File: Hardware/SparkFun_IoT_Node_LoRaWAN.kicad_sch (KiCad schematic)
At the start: 67 parts, among them J1 USB_C_Receptacle, J2 Conn_01x03, J3 USB_C_Receptacle, J4 SWD, SW1 DPDT_Slide_SMD_7.2x3.5mm, U1 RP2350A, U2 W25Q128JVPIM, U3 APS6404L-3SQR-ZR, U4 XBLR, U5 CH340C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

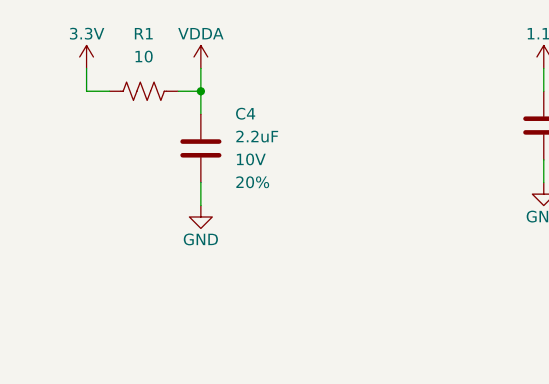
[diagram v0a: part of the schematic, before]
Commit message: Cosmetic tweaks
Nudge IO 29 silk away from mounting hole
Add VDDA RC filter cutoff frequency
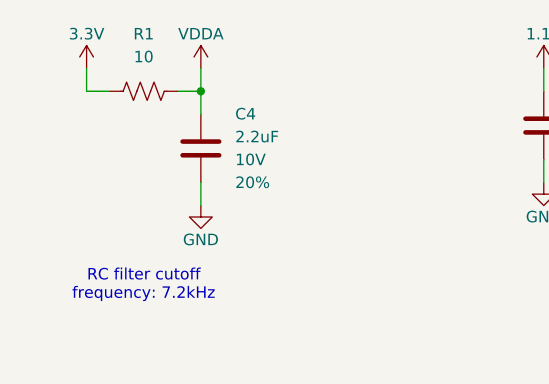
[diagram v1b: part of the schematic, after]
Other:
- note added: "RC filter cutoff frequency: 7.2kHz"
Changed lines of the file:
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@@
+		)
+	)
+	(text "RC filter cutoff\nfrequency: 7.2kHz"
+		(exclude_from_sim no)
+		(at 26.67 257.81 0)
+		(effects
+			(font
+				(size 1.27 1.27)
+			)
 		)
 	)

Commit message: Symbol and footprint update
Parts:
- J4: symbol SparkFun-Connector:Debug-Cortex-2x5-SMD-Unshrouded -> SparkFun-Connector:Debug-Cortex-2x5_P1.27mm-SMD-Unshrouded
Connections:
- net at J3.A8 (NC): no longer J3.B8 (NC)
- net at J1.A8 (NC): no longer J1.B8 (NC)
- now unconnected: J1.NC1 (NC), J1.NC2 (NC), J1.NC3 (NC), J3.NC1 (NC), J3.NC2 (NC), J3.NC3 (NC)
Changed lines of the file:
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@@
 	)
 	(symbol
-		(lib_name "USB_C_Receptacle_1")
 		(lib_id "SparkFun-Connector:USB_C_Receptacle")
 		(at 254 49.53 0)
@@
 	)
 	(symbol
-		(lib_name "VUSB_6")
 		(lib_id "SparkFun-PowerSymbol:VUSB")
 		(at 246.38 134.62 0)
@@
 	)
 	(symbol
-		(lib_name "GND_37")
 		(lib_id "SparkFun-PowerSymbol:GND")
 		(at 300.99 76.2 0)
@@
 	)
 	(symbol
-		(lib_name "GND_35")
 		(lib_id "SparkFun-PowerSymbol:GND")
 		(at 71.12 220.98 0)
@@
 	)
 	(symbol
-		(lib_name "GND_33")
 		(lib_id "SparkFun-PowerSymbol:GND")
 		(at 259.08 147.32 0)
@@
 	)
 	(symbol
-		(lib_name "GND_34")
 		(lib_id "SparkFun-PowerSymbol:GND")
 		(at 30.48 175.26 0)
@@
 	)
 	(symbol
-		(lib_name "3.3V_23")
 		(lib_id "SparkFun-PowerSymbol:3.3V")
 		(at 193.04 121.92 0)
@@
 	)
 	(symbol
-		(lib_name "GND_36")
 		(lib_id "SparkFun-PowerSymbol:GND")
 		(at 279.4 142.24 0)
@@
 	)
 	(symbol
-		(lib_name "GND_29")
 		(lib_id "SparkFun-PowerSymbol:GND")
 		(at 144.78 233.68 0)
@@
 	)
 	(symbol
-		(lib_name "3.3V_18")
 		(lib_id "SparkFun-PowerSymbol:3.3V")
 		(at 58.42 208.28 0)
@@
 	)
 	(symbol
-		(lib_name "3.3V_19")
 		(lib_id "SparkFun-PowerSymbol:3.3V")
 		(at 185.42 208.28 0)
@@
 	)
 	(symbol
-		(lib_name "Standoff_2")
 		(lib_id "SparkFun-Hardware:Standoff")
 		(at 400.05 242.57 0)
@@
 	)
 	(symbol
-		(lib_name "GND_23")
 		(lib_id "SparkFun-PowerSymbol:GND")
 		(at 40.64 73.66 0)
@@
 	)
 	(symbol
-		(lib_name "3.3V_20")
 		(lib_id "SparkFun-PowerSymbol:3.3V")
 		(at 83.82 208.28 0)
@@
 	)
 	(symbol
-		(lib_name "3.3V_22")
 		(lib_id "SparkFun-PowerSymbol:3.3V")
 		(at 152.4 134.62 0)
@@
 	)
 	(symbol
-		(lib_name "Standoff_3")
 		(lib_id "SparkFun-Hardware:Standoff")
 		(at 403.86 242.57 0)
@@
 	)
 	(symbol
-		(lib_name "GND_28")
 		(lib_id "SparkFun-PowerSymbol:GND")
 		(at 33.02 248.92 0)
@@
 	)
 	(symbol
-		(lib_name "GND_27")
 		(lib_id "SparkFun-PowerSymbol:GND")
 		(at 241.3 228.6 0)
@@
 	)
 	(symbol
-		(lib_id "SparkFun-Connector:Debug-Cortex-2x5-SMD-Unshrouded")
+		(lib_id "SparkFun-Connector:Debug-Cortex-2x5_P1.27mm-SMD-Unshrouded")
 		(at 378.46 53.34 0)
 		(unit 1)
@@
 	)
 	(symbol
-		(lib_name "VUSB_4")
 		(lib_id "SparkFun-PowerSymbol:VUSB")
 		(at 300.99 48.26 0)
@@
 	)
 	(symbol
-		(lib_name "GND_30")
 		(lib_id "SparkFun-PowerSymbol:GND")
 		(at 45.72 220.98 0)
@@
 	)
 	(symbol
-		(lib_name "VUSB_5")
 		(lib_id "SparkFun-PowerSymbol:VUSB")
 		(at 284.48 38.1 0)
@@
 	)
 	(symbol
-		(lib_name "Standoff_1")
 		(lib_id "SparkFun-Hardware:Standoff")
 		(at 403.86 238.76 0)
@@
 	)
 	(symbol
-		(lib_name "3.3V_21")
 		(lib_id "SparkFun-PowerSymbol:3.3V")
 		(at 259.08 134.62 0)
@@
 	)
 	(symbol
-		(lib_name "GND_26")
 		(lib_id "SparkFun-PowerSymbol:GND")
 		(at 309.88 139.7 0)
@@
 	)
 	(symbol
-		(lib_name "GND_24")
 		(lib_id "SparkFun-PowerSymbol:GND")
 		(at 254 73.66 0)
@@
 	)
 	(symbol
-		(lib_name "GND_32")
 		(lib_id "SparkFun-PowerSymbol:GND")
 		(at 82.55 76.2 0)
@@
 	)
 	(symbol
-		(lib_name "GND_25")
 		(lib_id "SparkFun-PowerSymbol:GND")
 		(at 33.02 220.98 0)
@@
 	)
 	(symbol
-		(lib_name "GND_31")
 		(lib_id "SparkFun-PowerSymbol:GND")
 		(at 266.7 259.08 0)
@@
 	)
 	(symbol
-		(lib_name "GND_19")
 		(lib_id "SparkFun-PowerSymbol:GND")
 		(at 109.22 220.98 0)
@@
 	)
 	(symbol
-		(lib_name "GND_12")
 		(lib_id "SparkFun-PowerSymbol:GND")
 		(at 152.4 147.32 0)
@@
 	)
 	(symbol
-		(lib_name "Fiducial_0.5mm_1")
 		(lib_id "SparkFun-Aesthetic:Fiducial_0.5mm")
 		(at 411.48 242.57 0)
@@
 	)
 	(symbol
-		(lib_name "SolderJumper_2_Bridged_1")
 		(lib_id "SparkFun-Jumper:SolderJumper_2_Bridged")
 		(at 36.83 71.12 0)
@@
 	)
 	(symbol
-		(lib_name "GND_20")
 		(lib_id "SparkFun-PowerSymbol:GND")
 		(at 58.42 73.66 0)
@@
 	)
 	(symbol
-		(lib_name "3.3V_7")
 		(lib_id "SparkFun-PowerSymbol:3.3V")
 		(at 45.72 208.28 0)
@@
 	)
 	(symbol
-		(lib_name "3.3V_15")
 		(lib_id "SparkFun-PowerSymbol:3.3V")
 		(at 365.76 45.72 0)
@@
 	)
 	(symbol
-		(lib_name "VUSB_3")
 		(lib_id "SparkFun-PowerSymbol:VUSB")
 		(at 271.78 38.1 0)
@@
 	)
 	(symbol
-		(lib_name "GND_21")
 		(lib_id "SparkFun-PowerSymbol:GND")
 		(at 279.4 259.08 0)
@@
 	)
 	(symbol
-		(lib_name "3.3V_14")
 		(lib_id "SparkFun-PowerSymbol:3.3V")
 		(at 109.22 208.28 0)
@@
 	)
 	(symbol
-		(lib_name "GND_13")
 		(lib_id "SparkFun-PowerSymbol:GND")
 		(at 71.12 246.38 0)
@@
 	)
 	(symbol
-		(lib_name "3.3V_17")
 		(lib_id "SparkFun-PowerSymbol:3.3V")
 		(at 241.3 170.18 0)
@@
 	)
 	(symbol
-		(lib_name "3.3V_9")
 		(lib_id "SparkFun-PowerSymbol:3.3V")
 		(at 241.3 243.84 0)
@@
 	)
 	(symbol
-		(lib_name "GND_18")
 		(lib_id "SparkFun-PowerSymbol:GND")
 		(at 83.82 246.38 0)
@@
 	)
 	(symbol
-		(lib_name "GND_16")
 		(lib_id "SparkFun-PowerSymbol:GND")
 		(at 96.52 246.38 0)
@@
 	)
 	(symbol
-		(lib_name "GND_11")
 		(lib_id "SparkFun-PowerSymbol:GND")
 		(at 160.02 149.86 0)
@@
 	)
 	(symbol
-		(lib_name "3.3V_8")
 		(lib_id "SparkFun-PowerSymbol:3.3V")
 		(at 160.02 218.44 0)
@@
 	)
 	(symbol
-		(lib_name "Fiducial_0.5mm_2")
 		(lib_id "SparkFun-Aesthetic:Fiducial_0.5mm")
 		(at 411.48 238.76 0)
@@
 	)
 	(symbol
-		(lib_name "GND_14")
 		(lib_id "SparkFun-PowerSymbol:GND")
 		(at 58.42 220.98 0)
@@
 	)
 	(symbol
-		(lib_name "3.3V_11")
 		(lib_id "SparkFun-PowerSymbol:3.3V")
 		(at 96.52 208.28 0)
@@
 	)
 	(symbol
-		(lib_name "VDDA_1")
 		(lib_id "SparkFun-PowerSymbol:VDDA")
 		(at 33.02 233.68 0)
@@
 	)
 	(symbol
-		(lib_name "3.3V_13")
 		(lib_id "SparkFun-PowerSymbol:3.3V")
 		(at 63.5 109.22 0)
@@
 	)
 	(symbol
-		(lib_name "GND_10")
 		(lib_id "SparkFun-PowerSymbol:GND")
 		(at 246.38 147.32 0)
@@
 	)
 	(symbol
-		(lib_name "GND_22")
 		(lib_id "SparkFun-PowerSymbol:GND")
 		(at 152.4 233.68 0)
@@
 	)
 	(symbol
-		(lib_name "3.3V_16")
 		(lib_id "SparkFun-PowerSymbol:3.3V")
 		(at 276.86 106.68 0)
@@
 	)
 	(symbol
-		(lib_name "GND_9")
 		(lib_id "SparkFun-PowerSymbol:GND")
 		(at 109.22 246.38 0)
@@
 	)
 	(symbol
-		(lib_name "3.3V_10")
 		(lib_id "SparkFun-PowerSymbol:3.3V")
 		(at 33.02 208.28 0)
@@
 	)
 	(symbol
-		(lib_name "GND_8")
 		(lib_id "SparkFun-PowerSymbol:GND")
 		(at 83.82 220.98 0)
@@
 	)
 	(symbol
-		(lib_name "3.3V_6")
 		(lib_id "SparkFun-PowerSymbol:3.3V")
 		(at 279.4 243.84 0)
@@
 	)
 	(symbol
-		(lib_name "3.3V_12")
 		(lib_id "SparkFun-PowerSymbol:3.3V")
 		(at 160.02 132.08 0)
@@
 	)
 	(symbol
-		(lib_name "GND_7")
 		(lib_id "SparkFun-PowerSymbol:GND")
 		(at 271.78 73.66 0)
@@
 	)
 	(symbol
-		(lib_name "GND_17")
 		(lib_id "SparkFun-PowerSymbol:GND")
 		(at 20.32 220.98 0)
@@
 	)
 	(symbol
-		(lib_name "GND_15")
 		(lib_id "SparkFun-PowerSymbol:GND")
 		(at 365.76 58.42 0)
@@
 	)
 	(symbol
-		(lib_name "Fiducial_0.5mm_3")
 		(lib_id "SparkFun-Aesthetic:Fiducial_0.5mm")
 		(at 415.29 238.76 0)
@@
 	)
 	(symbol
-		(lib_name "VUSB_2")
 		(lib_id "SparkFun-PowerSymbol:VUSB")
 		(at 279.4 104.14 0)
@@
 	)
 	(symbol
-		(lib_name "3.3V_5")
 		(lib_id "SparkFun-PowerSymbol:3.3V")
 		(at 20.32 233.68 0)
@@
 	)
 	(symbol
-		(lib_name "3.3V_4")
 		(lib_id "SparkFun-PowerSymbol:3.3V")
 		(at 233.68 180.34 0)
@@
 	)
 	(symbol
-		(lib_name "GND_6")
 		(lib_id "SparkFun-PowerSymbol:GND")
 		(at 281.94 73.66 0)
@@
 	)
 	(symbol
-		(lib_name "GND_5")
 		(lib_id "SparkFun-PowerSymbol:GND")
 		(at 63.5 187.96 0)
@@
 	)
 	(symbol
-		(lib_name "3.3V_1")
 		(lib_id "SparkFun-PowerSymbol:3.3V")
 		(at 152.4 220.98 0)
@@
 	)
 	(symbol
-		(lib_name "GND_1")
 		(lib_id "SparkFun-PowerSymbol:GND")
 		(at 63.5 73.66 0)
@@
 	)
 	(symbol
-		(lib_name "3.3V_3")
 		(lib_id "SparkFun-PowerSymbol:3.3V")
 		(at 71.12 208.28 0)
@@
 	)
 	(symbol
-		(lib_name "GND_3")
 		(lib_id "SparkFun-PowerSymbol:GND")
 		(at 254 259.08 0)
@@
 	)
 	(symbol
-		(lib_name "GND_4")
 		(lib_id "SparkFun-PowerSymbol:GND")
 		(at 96.52 220.98 0)
@@
 	)
 	(symbol
-		(lib_name "GND_2")
 		(lib_id "SparkFun-PowerSymbol:GND")
 		(at 170.18 55.88 0)
@@
 	)
 	(symbol
-		(lib_name "VUSB_1")
 		(lib_id "SparkFun-PowerSymbol:VUSB")
 		(at 82.55 48.26 0)
@@
 	)
 	(symbol
-		(lib_name "3.3V_2")
 		(lib_id "SparkFun-PowerSymbol:3.3V")
 		(at 144.78 220.98 0)

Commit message: Design review updates
Fix layers to standard SFE usage
Add link to enclosure and PDF of dimensions
Move fiducials away from PTH pads
Add USB test points
Add XBLR debug test points
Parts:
- added TP10, TP3, TP4, TP5, TP6, TP7, TP8, TP9: 1.0mm, SparkFun-Connector:TestPoint-1.0mm, symbol SparkFun-Connector:TestPoint_1.0mm
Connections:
- net USB_D+: now also TP4.1
- net USB_D-: now also TP3.1
- net XBLR_SWCLK: now also TP6.1
- net XBLR_SWDIO: now also TP7.1
- net XBLR_SWO: now also TP5.1
- net XBLR_USB_D+: now also TP10.1
- net XBLR_USB_D-: now also TP9.1
- net XBLR_~{RESET}: now also TP8.1
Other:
- moved on the sheet: J4

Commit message: Add XBLR 3D model
Also fix RP2350A library reference
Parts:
- U1: footprint SparkFun_IoT_Node_LoRaWAN:RP2350A -> SparkFun-Semiconductor-Standard:QFN-60-1EP_7x7mm_P0.4mm_EP3.5x3.5mm; symbol SparkFun_IoT_Node_LoRaWAN:RP2350A -> SparkFun-IC-Microcontroller:RP2350A
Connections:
- net GND: now also U1.EP (GND); no longer U1.EPAD (GND)
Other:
- moved on the sheet: U1
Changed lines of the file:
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@@
 	)
 	(symbol
-		(lib_id "SparkFun_IoT_Node_LoRaWAN:RP2350A")
+		(lib_id "SparkFun-IC-Microcontroller:RP2350A")
 		(at 83.82 149.86 0)
 		(unit 1)
@@
 			)
 		)
-		(property "Footprint" "SparkFun_IoT_Node_LoRaWAN:RP2350A"
+		(property "Footprint" "SparkFun-Semiconductor-Standard:QFN-60-1EP_7x7mm_P0.4mm_EP3.5x3.5mm"
 			(at 83.82 187.96 0)
 			(effects
@@
 			)
 		)
-		(property "Datasheet" "~"
+		(property "Datasheet" "https://datasheets.raspberrypi.com/rp2350/rp2350-datasheet.pdf"
 			(at 83.82 193.04 0)
 			(effects
@@
 		)
 		(property "Description" "Raspberry Pi RP2350A 150MHz Dual ARM Cortex-M33 Microcontroller IC QFN-60"
-			(at 83.82 149.86 0)
+			(at 83.82 195.58 0)
 			(effects
 				(font
@@
 		(pin "8"
 		)
-		(pin "EPAD"
+		(pin "EP"
 		)
 		(pin "7"

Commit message: Set XBLR debug header to DNP
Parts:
- J4: now not fitted
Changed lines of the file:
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@@
 		(in_bom yes)
 		(on_board yes)
-		(dnp no)
+		(dnp yes)
 		(fields_autoplaced yes)
 		(property "Reference" "J4"
